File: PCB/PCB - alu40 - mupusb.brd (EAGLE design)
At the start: 228 x 76 mm, 159 parts, among them IC1 XB3303ASOT23, IC2 TP4054-42-SOT25-R, J1 SK-3296S-01-L1, Q2 PMOSFET, Q3 PMOSFET, Q5 PMOSFET, Q6 NMOSFET, U1 ISP1807-LRISP1807-LR_ISP1807-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, X1 BM02B-SRSS-TB

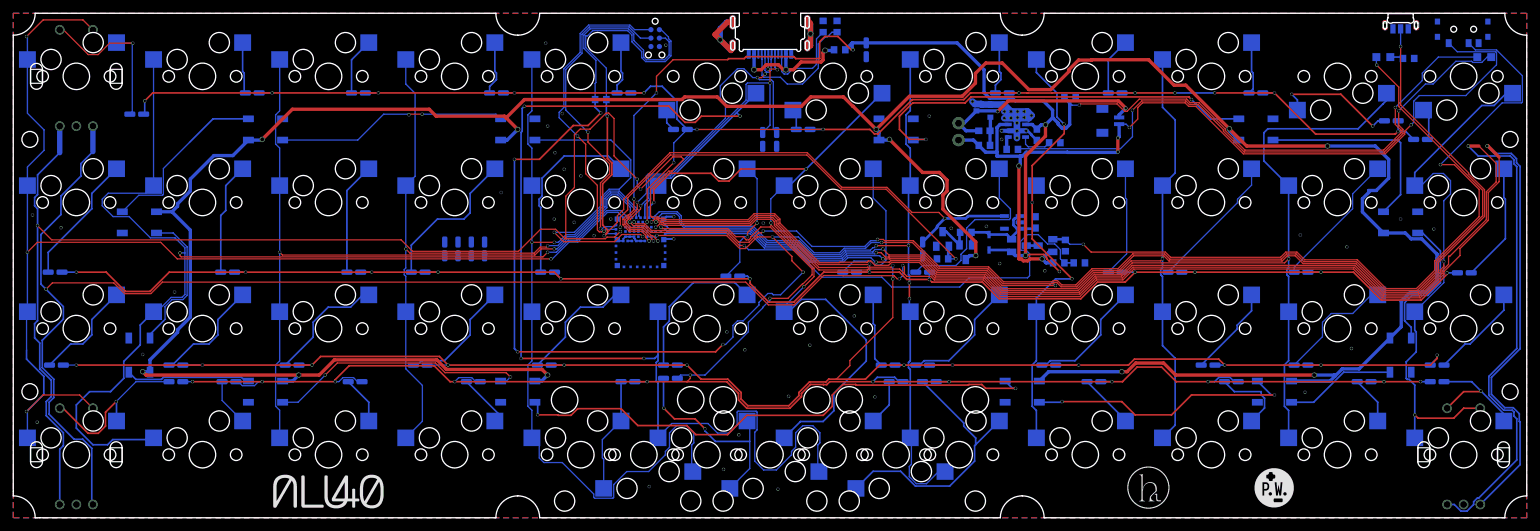
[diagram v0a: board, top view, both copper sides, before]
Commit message: Move LEDs across bottom
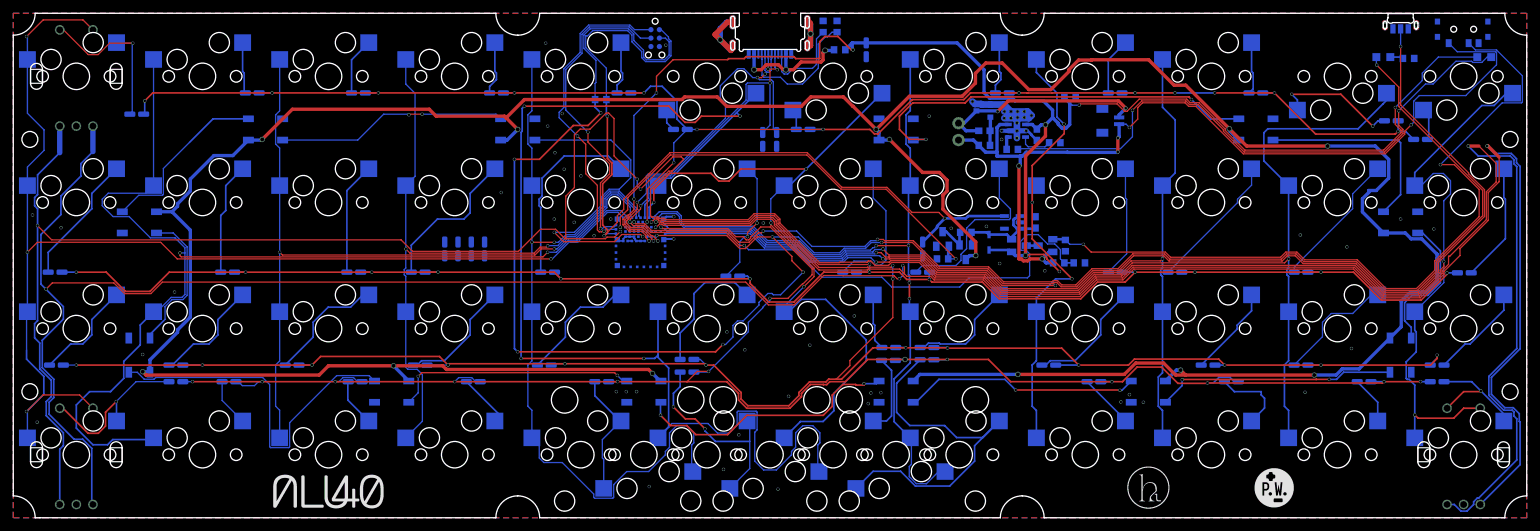
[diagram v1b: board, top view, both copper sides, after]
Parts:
- moved D81 19.0 mm to (57.0, 19.0)
- moved D82 19.0 mm to (95.0, 19.0)
- moved D83 19.0 mm to (133.0, 19.0)
- moved D84 19.0 mm to (171.0, 19.0)
- moved D41 3.95 mm to (88.7, 20.5)
- moved D48 3.40 mm to (131.8, 23.7)
- moved D43 3.32 mm to (137.7, 23.8)
- moved D32 2.73 mm to (137.7, 25.6)
- moved D42 2.67 mm to (101.5, 21.9)
- moved D31 2.65 mm to (131.9, 25.6)
- moved D30 2.64 mm to (101.5, 23.9)
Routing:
- net N$85: track 82.6 -> 40.7 mm
- net N$81: track 18.8 -> 54.4 mm
- net V_WS2812: track 453.5 -> 484.4 mm, vias 12 -> 13
- net N$87: track 16.7 -> 36.2 mm, vias 0 -> 2
- net N$43: track 41.8 -> 56.5 mm
- net N$86: track 41.0 -> 35.5 mm
- net N$1: track 6.92 -> 12.1 mm
- net ROW3: track 284.1 -> 281.0 mm
- net N$30: track 23.2 -> 20.3 mm
- net N$84: track 39.4 -> 36.7 mm
- net N$31: track 11.1 -> 8.47 mm
- net ROW2: track 301.2 -> 303.2 mm
- net COL7: track 113.2 -> 115.0 mm
- net N$32: track 18.3 -> 16.7 mm
- net N$41: track 17.4 -> 19.0 mm
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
